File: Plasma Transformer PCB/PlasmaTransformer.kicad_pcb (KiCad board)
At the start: 2 copper layers, 90 x 90 mm, 86 parts, among them J1 Barrel_Jack_MountingPin, J10 Conn_01x01_Socket, J11 Screw_Terminal_01x01, J12 Screw_Terminal_01x01, J13 Conn_01x01_Socket, J14 Conn_01x01_Socket, J15 Conn_01x01_Socket, J16 Conn_01x01_Socket, J17 Conn_01x01_Socket, J18 Conn_01x01_Socket, J19 Conn_01x01_Socket, J2 Conn_01x02_Pin, J20 Conn_01x01_Socket, J21 Conn_01x01_Socket, J3 Conn_Coaxial, J4 Conn_02x04_Odd_Even, J5 Conn_Coaxial, J6 Conn_02x04_Odd_Even, J7 Conn_01x01_Socket, J8 AudioJack3, J9 Conn_01x01_Socket, M1 Fan, Q1 Q_NMOS_Depletion_GDS, SW1 SW_SPDT, T1 BO-02, T2 ZS 1052-S HT(H), U1 LMR51610YDBVR

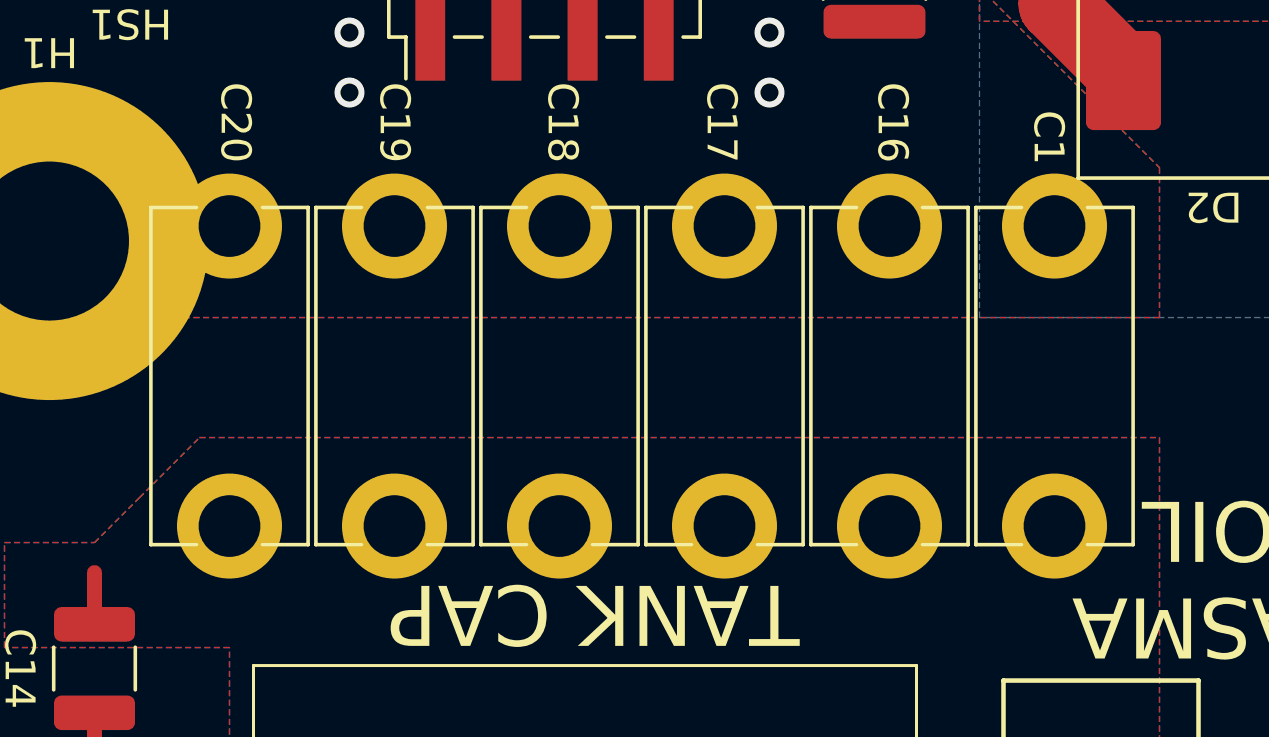
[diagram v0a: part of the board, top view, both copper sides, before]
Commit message: updated hole size for capacitor press fit sockets
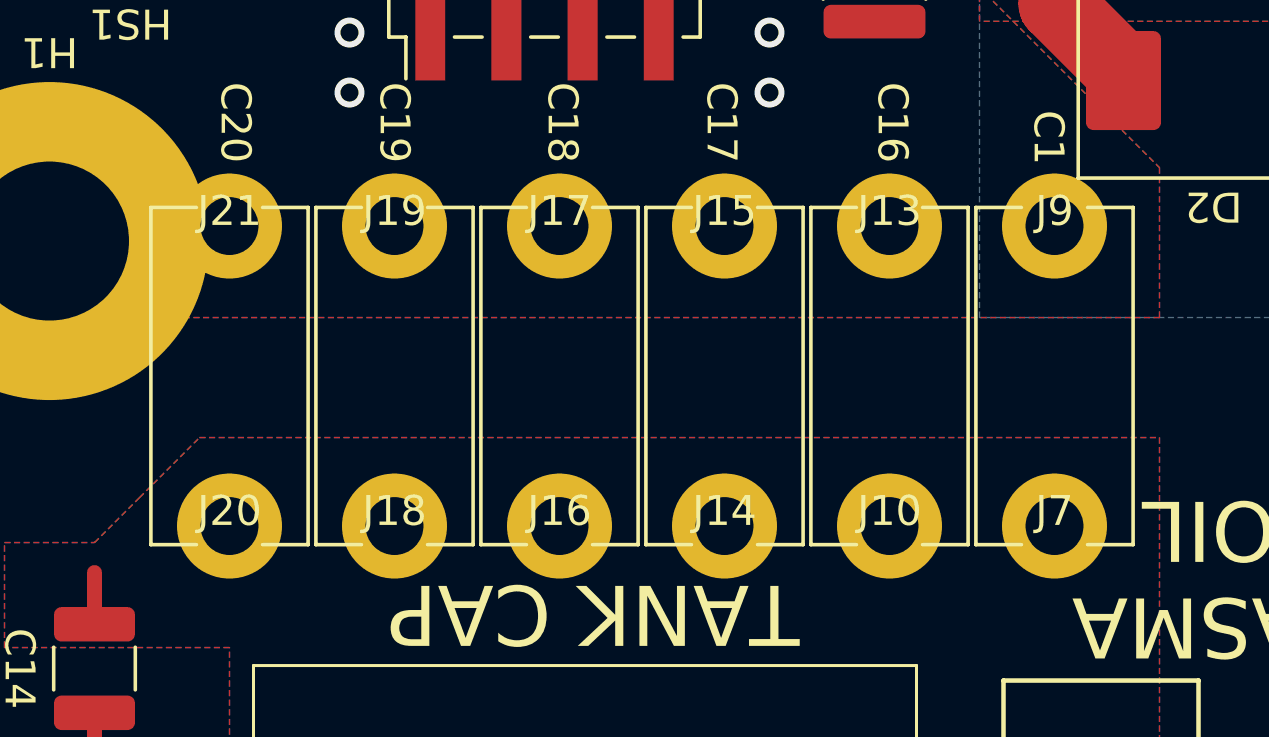
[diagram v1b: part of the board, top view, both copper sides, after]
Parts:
- H1: value MountingHole_Pad -> Pad_Doorknob_Cap
- H2: value MountingHole -> Hole_Heatsink_Screw
- J10, J13, J14, J15, J16, J17, J18, J19, J20, J21, J7, J9: footprint ALibrary:H8501-05 -> AFootprints:H8501-05
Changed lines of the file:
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@@
 		)
 	)
-	(footprint "ALibrary:H8501-05"
+	(footprint "AFootprints:H8501-05"
 		(layer "F.Cu")
 		(at 89 111.45)
@@
 			(unlocked yes)
 			(layer "F.SilkS")
-			(hide yes)
 			(effects
 				(font
@@
 			(at 0 0)
 			(size 3.5 3.5)
-			(drill 2.057)
+			(drill 1.9304)
 			(layers "*.Cu" "*.Mask")
 			(remove_unused_layers no)
@@
 		)
 	)
-	(footprint "ALibrary:H8501-05"
+	(footprint "AFootprints:H8501-05"
 		(layer "F.Cu")
 		(at 83.5 121.45)
@@
 			(unlocked yes)
 			(layer "F.SilkS")
-			(hide yes)
 			(effects
 				(font
@@
 			(at 0 0)
 			(size 3.5 3.5)
-			(drill 2.057)
+			(drill 1.9304)
 			(layers "*.Cu" "*.Mask")
 			(remove_unused_layers no)
@@
 			)
 		)
+		(property "Tolerance" "1%"
+			(at 0 0 180)
+			(unlocked yes)
+			(layer "F.Fab")
+			(hide yes)
+			(effects
+				(font
+					(size 1 1)
+					(thickness 0.15)
+				)
+			)
+		)
 		(property ki_fp_filters "R_*")
 		(sheetname "/")
@@
 		)
 	)
-	(footprint "ALibrary:H8501-05"
+	(footprint "AFootprints:H8501-05"
 		(layer "F.Cu")
 		(at 83.5 111.45)
@@
 			(unlocked yes)
 			(layer "F.SilkS")
-			(hide yes)
 			(effects
 				(font
@@
 			(at 0 0)
 			(size 3.5 3.5)
-			(drill 2.057)
+			(drill 1.9304)
 			(layers "*.Cu" "*.Mask")
 			(remove_unused_layers no)
@@
 		)
 	)
-	(footprint "ALibrary:H8501-05"
+	(footprint "AFootprints:H8501-05"
 		(layer "F.Cu")
 		(at 67 111.45)
@@
 			(unlocked yes)
 			(layer "F.SilkS")
-			(hide yes)
 			(effects
 				(font
@@
 			(at 0 0)
 			(size 3.5 3.5)
-			(drill 2.057)
+			(drill 1.9304)
 			(layers "*.Cu" "*.Mask")
 			(remove_unused_layers no)
@@
 			)
 		)
-		(property "Value" "MountingHole"
+		(property "Value" "Hole_Heatsink_Screw"
 			(at 0 9.4 0)
 			(layer "F.Fab")
@@
 			)
 		)
+		(property "Tolerance" "1%"
+			(at 0 0 270)
+			(unlocked yes)
+			(layer "F.Fab")
+			(hide yes)
+			(effects
+				(font
+					(size 1 1)
+					(thickness 0.15)
+				)
+			)
+		)
 		(property ki_fp_filters "R_*")
 		(sheetname "/")
@@
 			)
 		)
+		(property "Tolerance" "1%"
+			(at 0 0 0)
+			(unlocked yes)
+			(layer "F.Fab")
+			(hide yes)
+			(effects
+				(font
+					(size 1 1)
+					(thickness 0.15)
+				)
+			)
+		)
 		(property ki_fp_filters "R_*")
 		(sheetname "/")
@@
 		)
 	)
-	(footprint "ALibrary:H8501-05"
+	(footprint "AFootprints:H8501-05"
 		(layer "F.Cu")
 		(at 94.5 121.45)
@@
 			(unlocked yes)
 			(layer "F.SilkS")
-			(hide yes)
 			(effects
 				(font
@@
 			(at 0 0)
 			(size 3.5 3.5)
-			(drill 2.057)
+			(drill 1.9304)
 			(layers "*.Cu" "*.Mask")
 			(remove_unused_layers no)
@@
 		)
 	)
-	(footprint "ALibrary:H8501-05"
+	(footprint "AFootprints:H8501-05"
 		(layer "F.Cu")
 		(at 78 121.45)
@@
 			(unlocked yes)
 			(layer "F.SilkS")
-			(hide yes)
 			(effects
 				(font
@@
 			(at 0 0)
 			(size 3.5 3.5)
-			(drill 2.057)
+			(drill 1.9304)
 			(layers "*.Cu" "*.Mask")
 			(remove_unused_layers no)
@@
 			)
 		)
-		(property "Description" "Capacitor 1111"
+		(property "Description" "Capacitor 1111 (1210 footprint compatible)"
 			(at 0 0 270)
 			(unlocked yes)
@@
 		)
 	)
-	(footprint "ALibrary:H8501-05"
+	(footprint "AFootprints:H8501-05"
 		(layer "F.Cu")
 		(at 94.5 111.45)
@@
 			(unlocked yes)
 			(layer "F.SilkS")
-			(hide yes)
 			(effects
 				(font
@@
 			(at 0 0)
 			(size 3.5 3.5)
-			(drill 2.057)
+			(drill 1.9304)
 			(layers "*.Cu" "*.Mask")
 			(remove_unused_layers no)
@@
 			)
 		)
+		(property "Tolerance" "1%"
+			(at 0 0 270)
+			(unlocked yes)
+			(layer "F.Fab")
+			(hide yes)
+			(effects
+				(font
+					(size 1 1)
+					(thickness 0.15)
+				)
+			)
+		)
 		(property ki_fp_filters "R_*")
 		(sheetname "/")
@@
 		)
 	)
-	(footprint "ALibrary:H8501-05"
+	(footprint "AFootprints:H8501-05"
 		(layer "F.Cu")
 		(at 78 111.45)
@@
 			(unlocked yes)
 			(layer "F.SilkS")
-			(hide yes)
 			(effects
 				(font
@@
 			(at 0 0)
 			(size 3.5 3.5)
-			(drill 2.057)
+			(drill 1.9304)
 			(layers "*.Cu" "*.Mask")
 			(remove_unused_layers no)
@@
 			)
 		)
+		(property "Tolerance" "1%"
+			(at 0 0 90)
+			(unlocked yes)
+			(layer "F.Fab")
+			(hide yes)
+			(effects
+				(font
+					(size 1 1)
+					(thickness 0.15)
+				)
+			)
+		)
 		(property ki_fp_filters "R_*")
 		(sheetname "/")
@@
 			)
 		)
-		(property "Description" "Capacitor 1111"
+		(property "Description" "Capacitor 1111 (1210 footprint compatible)"
 			(at 0 0 270)
 			(unlocked yes)
@@
 			)
 		)
-		(property "Value" "MountingHole_Pad"
+		(property "Value" "Pad_Doorknob_Cap"
 			(at 0 6.3 0)
 			(layer "F.Fab")
@@
 			)
 		)
+		(property "Tolerance" "1%"
+			(at 0 0 270)
+			(unlocked yes)
+			(layer "F.Fab")
+			(hide yes)
+			(effects
+				(font
+					(size 1 1)
+					(thickness 0.15)
+				)
+			)
+		)
 		(property ki_fp_filters "R_*")
 		(sheetname "/")
@@
 		)
 	)
-	(footprint "ALibrary:H8501-05"
+	(footprint "AFootprints:H8501-05"
 		(layer "F.Cu")
 		(at 89 121.45)
@@
 			(unlocked yes)
 			(layer "F.SilkS")
-			(hide yes)
 			(effects
 				(font
@@
 			(at 0 0)
 			(size 3.5 3.5)
-			(drill 2.057)
+			(drill 1.9304)
 			(layers "*.Cu" "*.Mask")
 			(remove_unused_layers no)
@@
 			)
 		)
-		(property "Description" "Heatsink"
+		(property "Description" "Heatsink, dxf in repo for drill and tap layout"
 			(at 0 0 0)
 			(unlocked yes)
@@
 		)
 	)
-	(footprint "ALibrary:H8501-05"
+	(footprint "AFootprints:H8501-05"
 		(layer "F.Cu")
 		(at 67 121.45)
@@
 			(unlocked yes)
 			(layer "F.SilkS")
-			(hide yes)
 			(effects
 				(font
@@
 			(at 0 0)
 			(size 3.5 3.5)
-			(drill 2.057)
+			(drill 1.9304)
 			(layers "*.Cu" "*.Mask")
 			(remove_unused_layers no)
@@
 			)
 		)
+		(property "Tolerance" "1%"
+			(at 0 0 270)
+			(unlocked yes)
+			(layer "F.Fab")
+			(hide yes)
+			(effects
+				(font
+					(size 1 1)
+					(thickness 0.15)
+				)
+			)
+		)
 		(property ki_fp_filters "R_*")
 		(sheetname "/")
@@
 		)
 	)
-	(footprint "ALibrary:H8501-05"
+	(footprint "AFootprints:H8501-05"
 		(layer "F.Cu")
 		(at 72.5 111.45)
@@
 			(unlocked yes)
 			(layer "F.SilkS")
-			(hide yes)
 			(effects
 				(font
@@
 			(at 0 0)
 			(size 3.5 3.5)
-			(drill 2.057)
+			(drill 1.9304)
 			(layers "*.Cu" "*.Mask")
 			(remove_unused_layers no)
@@
 			)
 		)
+		(property "Tolerance" "1%"
+			(at 0 0 180)
+			(unlocked yes)
+			(layer "F.Fab")
+			(hide yes)
+			(effects
+				(font
+					(size 1 1)
+					(thickness 0.15)
+				)
+			)
+		)
 		(property ki_fp_filters "R_*")
 		(sheetname "/")
@@
 			)
 		)
-		(property "Description" "Capacitor 1111"
+		(property "Description" "Capacitor 1111 (1210 footprint compatible)"
 			(at 0 0 270)
 			(unlocked yes)
@@
 			)
 		)
+		(property "Tolerance" "1%"
+			(at 0 0 180)
+			(unlocked yes)
+			(layer "F.Fab")
+			(hide yes)
+			(effects
+				(font
+					(size 1 1)
+					(thickness 0.15)
+				)
+			)
+		)
 		(property ki_fp_filters "R_*")
 		(sheetname "/")
@@
 		)
 	)
-	(footprint "ALibrary:H8501-05"
+	(footprint "AFootprints:H8501-05"
 		(layer "F.Cu")
 		(at 72.5 121.45)
@@
 			(unlocked yes)
 			(layer "F.SilkS")
-			(hide yes)
 			(effects
 				(font
@@
 			(at 0 0)
 			(size 3.5 3.5)
-			(drill 2.057)
+			(drill 1.9304)
 			(layers "*.Cu" "*.Mask")
 			(remove_unused_layers no)
@@
 			)
 		)
-		(property "Description" "Capacitor 1111"
+		(property "Description" "Capacitor 1111 (1210 footprint compatible)"
 			(at 0 0 270)
 			(unlocked yes)
